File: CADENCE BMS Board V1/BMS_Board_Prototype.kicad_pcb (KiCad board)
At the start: 4 copper layers, 97 x 97 mm, 174 parts, among them IC1 R5432V407BA, J1 Screw_Terminal_01x02, J10 Conn_01x08, J11 Conn_01x06, J12 Conn_01x02, J13 Conn_01x08, J14 Conn_01x04, J15 Conn_01x08, J2 Conn_01x02, J20 Conn_01x02, J21 Conn_01x02, J28 Banana Socket PWR, J29 Banana Socket VSS, J3 Conn_01x08, J4 Conn_01x02, J5 Conn_01x01_Socket, J6 Conn_01x01_Socket, J7 Conn_01x01_Socket, J8 Conn_01x01_Socket, J9 Conn_01x04, Q1 P-Channel FET, Q10 N-MOS, Q2 60V Enhancement, Q3 60V Enhancement, Q4 60V Enhancement, Q5 Q_NMOS_DSG, Q6 Q_NMOS_DSG, Q7 Q_NMOS_DSG, Q8 N-MOS, Q9 N-MOS, U1 TVS2200DRV, U2 LT8612, U3 LT3652IMSE#PBF, U4 BQ34Z100-R2, U5 MCP9600-E_MX, U7 P82B715DR

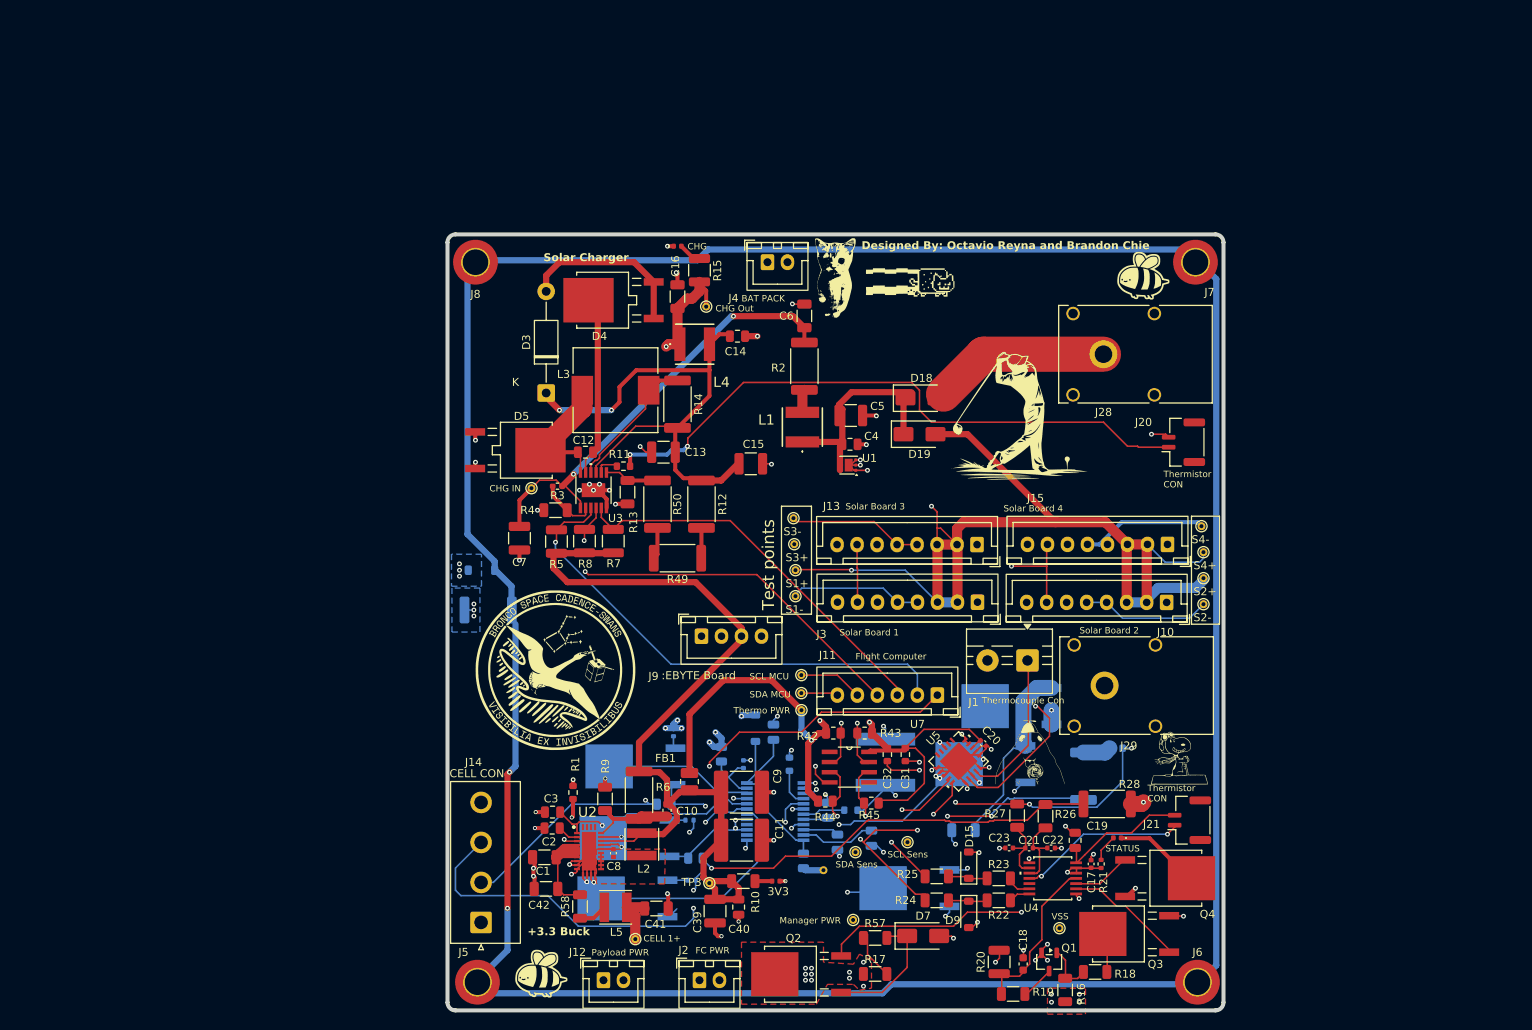
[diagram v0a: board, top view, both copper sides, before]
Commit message: Updates for USB-C charging and set up for testing
Revamped USB-C layout to make it cleaner and more compressed and also included schematic parts for adding in Banana plugs for testing the PCB
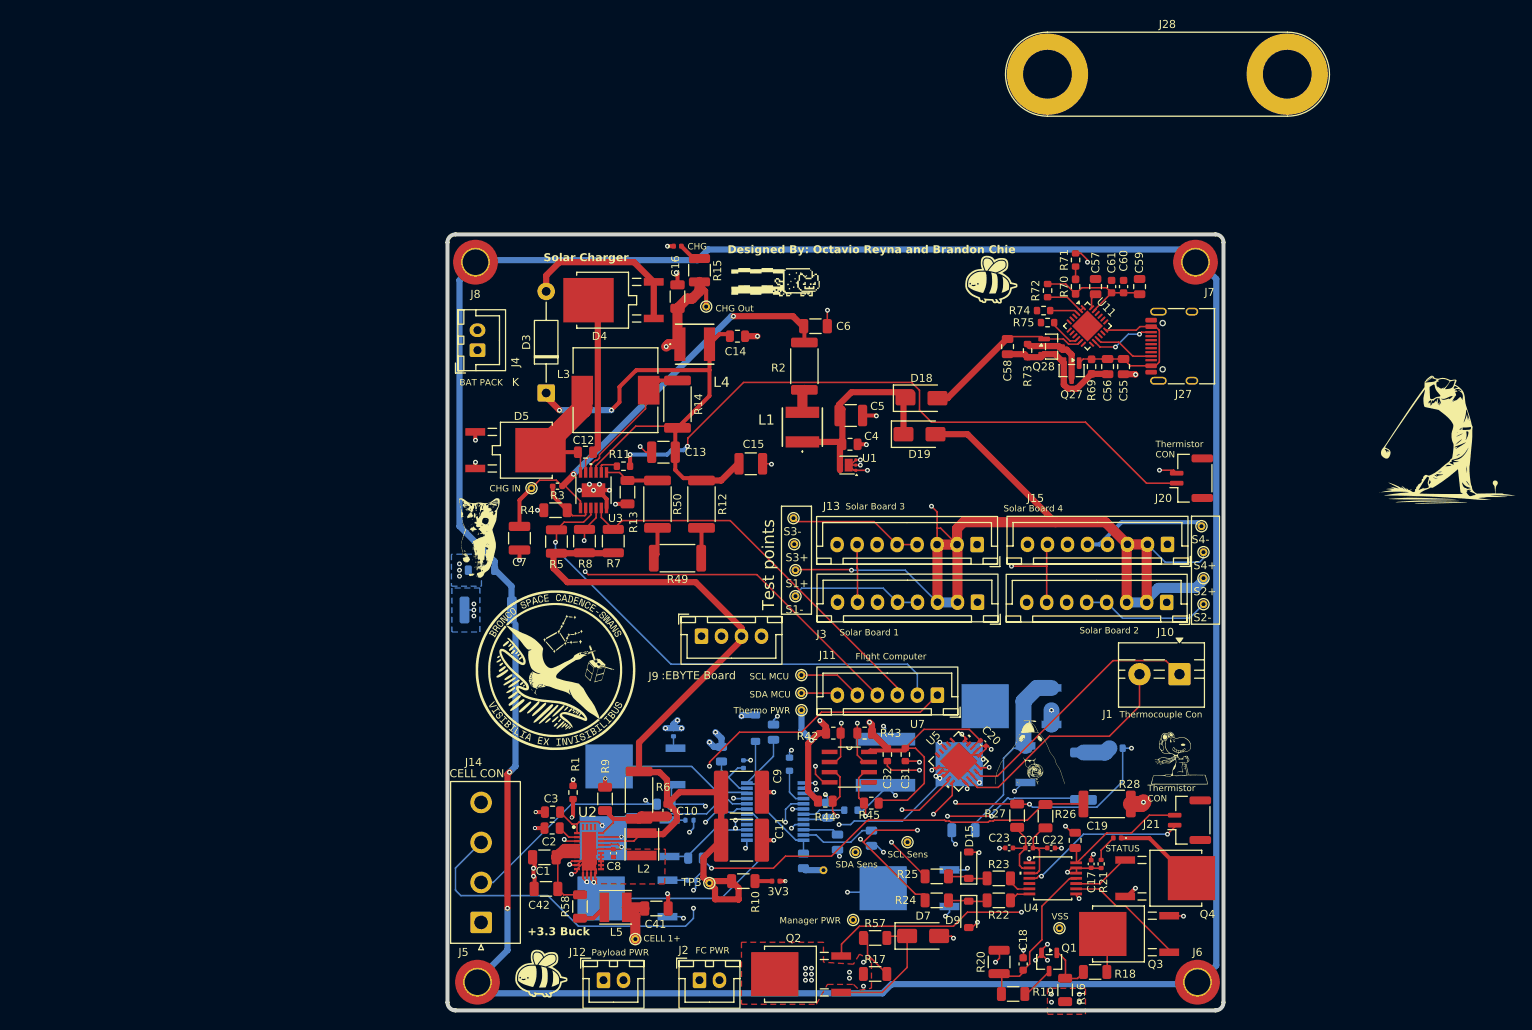
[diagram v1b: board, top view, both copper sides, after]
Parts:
- removed C39: 10uF, Capacitor_SMD:C_1210_3225Metric
- removed C40: 10nF, Capacitor_SMD:C_0805_2012Metric
- removed FB1: 600, Inductor_SMD:L_1008_2520Metric
- removed J29: Banana Socket VSS, Connector:Banana_Cliff_FCR7350B_S16N-PC_Horizontal
- added C55: 3.3uF, Capacitor_SMD:C_0805_2012Metric, F.Cu at (109.5, 36.5)
- added C56: 1uF, Capacitor_SMD:C_0805_2012Metric, F.Cu at (107.5, 36.5)
- added C57: 1uF, Capacitor_SMD:C_0805_2012Metric, F.Cu at (106.0, 26.5)
- added C58: 1uF, Capacitor_SMD:C_0805_2012Metric, F.Cu at (95.0, 34.0)
- added C59: 1uF, Capacitor_SMD:C_0805_2012Metric, F.Cu at (111.5, 26.5)
- added C60: 100nF, Capacitor_SMD:C_0603_1608Metric, F.Cu at (109.5, 26.5)
- added C61: 100nF, Capacitor_SMD:C_0603_1608Metric, F.Cu at (108.0, 26.5)
- added J27: USB_C_Receptacle_USB2.0_16P, Connector_USB:USB_C_Receptacle_HRO_TYPE-C-31-M-12, F.Cu at (117.0, 34.0)
- added Q27: Q_PMOS_DGS, Package_TO_SOT_SMD:SOT-23, F.Cu at (103.0, 37.0)
- added Q28: Q_PMOS_DGS, Package_TO_SOT_SMD:SOT-23, F.Cu at (100.5, 34.0)
- added R69: 10K, Resistor_SMD:R_0603_1608Metric_Pad0.98x0.95mm_HandSolder, F.Cu at (105.5, 36.5)
- added R70: 5.1K, Resistor_SMD:R_0603_1608Metric_Pad0.98x0.95mm_HandSolder, F.Cu at (103.5, 26.5)
- added R71: 2.4K, Resistor_SMD:R_0603_1608Metric, F.Cu at (103.5, 23.2)
- added R72: 0, Resistor_SMD:R_0603_1608Metric, F.Cu at (100.0, 27.0)
- added R73: 49.9K, Resistor_SMD:R_0603_1608Metric, F.Cu at (97.5, 34.5)
- added R74: 49.9K, Resistor_SMD:R_0603_1608Metric, F.Cu at (99.5, 29.5)
- added R75: 10K, Resistor_SMD:R_0603_1608Metric, F.Cu at (100.0, 31.0)
- added U11: CYPD3177-24LQ, Package_DFN_QFN:QFN-24-1EP_4x4mm_P0.5mm_EP2.75x2.75mm, F.Cu at (105.0, 31.5)
- J28: value Banana Socket PWR -> Banana Jack CON; footprint Connector:Banana_Cliff_FCR7350R_S16N-PC_Horizontal -> Connector:Banana_Jack_2Pin
- moved G*** 55.1 mm to (29.0, 58.0)
- moved G*** 53.6 mm to (149.5, 45.5)
- moved J4 37.9 mm to (28.8, 34.5), turned to 90 degrees
- moved J28 35.7 mm to (100.0, 0.00), turned to 0 degrees
- moved J1 19.1 mm to (116.5, 75.0)
- moved G*** 19.0 mm to (93.0, 25.5)
- moved G*** 16.8 mm to (65.2, 25.7)
- moved J20 4.61 mm to (118.0, 50.5)
- moved C6 1.89 mm to (71.0, 31.5), turned to 0 degrees
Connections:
- C20 pad 2: +3.3V Q -> +3.3V
- C31 pad 1: +3.3V Q -> +3.3V
- C32 pad 1: +3.3V Q -> +3.3V
- D18 pad 2: Net-(D18-A) -> VDC_OUT
- J28 pad 1: Net-(D18-A) -> Cell 3-
- R42 pad 1: +3.3V Q -> +3.3V
- R43 pad 1: +3.3V Q -> +3.3V
- R44 pad 1: +3.3V Q -> +3.3V
- R45 pad 1: +3.3V Q -> +3.3V
- TP7 pad 1: +3.3V Q -> +3.3V
- U5 pad 8: +3.3V Q -> +3.3V
- U7 pad 8: +3.3V Q -> +3.3V
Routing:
- net +3.3V Q: track 81.9 -> 0.00 mm, vias 3 -> 0
- net +3.3V: track 112.8 -> 163.4 mm, vias 0 -> 3
- net Net-(D18-A): track 22.1 -> 0.00 mm
- net VDC_OUT: track 0.00 -> 21.6 mm
- net VBUS: track 0.00 -> 21.3 mm
- net Net-(Q27-G): track 0.00 -> 16.9 mm
- net VDDD: track 0.00 -> 15.8 mm
- net Net-(J1-Pin_1): track 19.0 -> 32.4 mm
- net Net-(Q27-S): track 0.00 -> 8.99 mm
- net CC2: track 0.00 -> 8.14 mm, vias 0 -> 2
- net CC1: track 0.00 -> 7.65 mm
- net Net-(U11-VBUS_MAX): track 0.00 -> 5.31 mm
- net Net-(U11-FLIP): track 0.00 -> 4.20 mm
- net Net-(J1-Pin_2): track 26.3 -> 30.0 mm, vias 1 -> 0
- net VBUS_EN: track 0.00 -> 3.59 mm
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
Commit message: New connectors and adding in a test setup
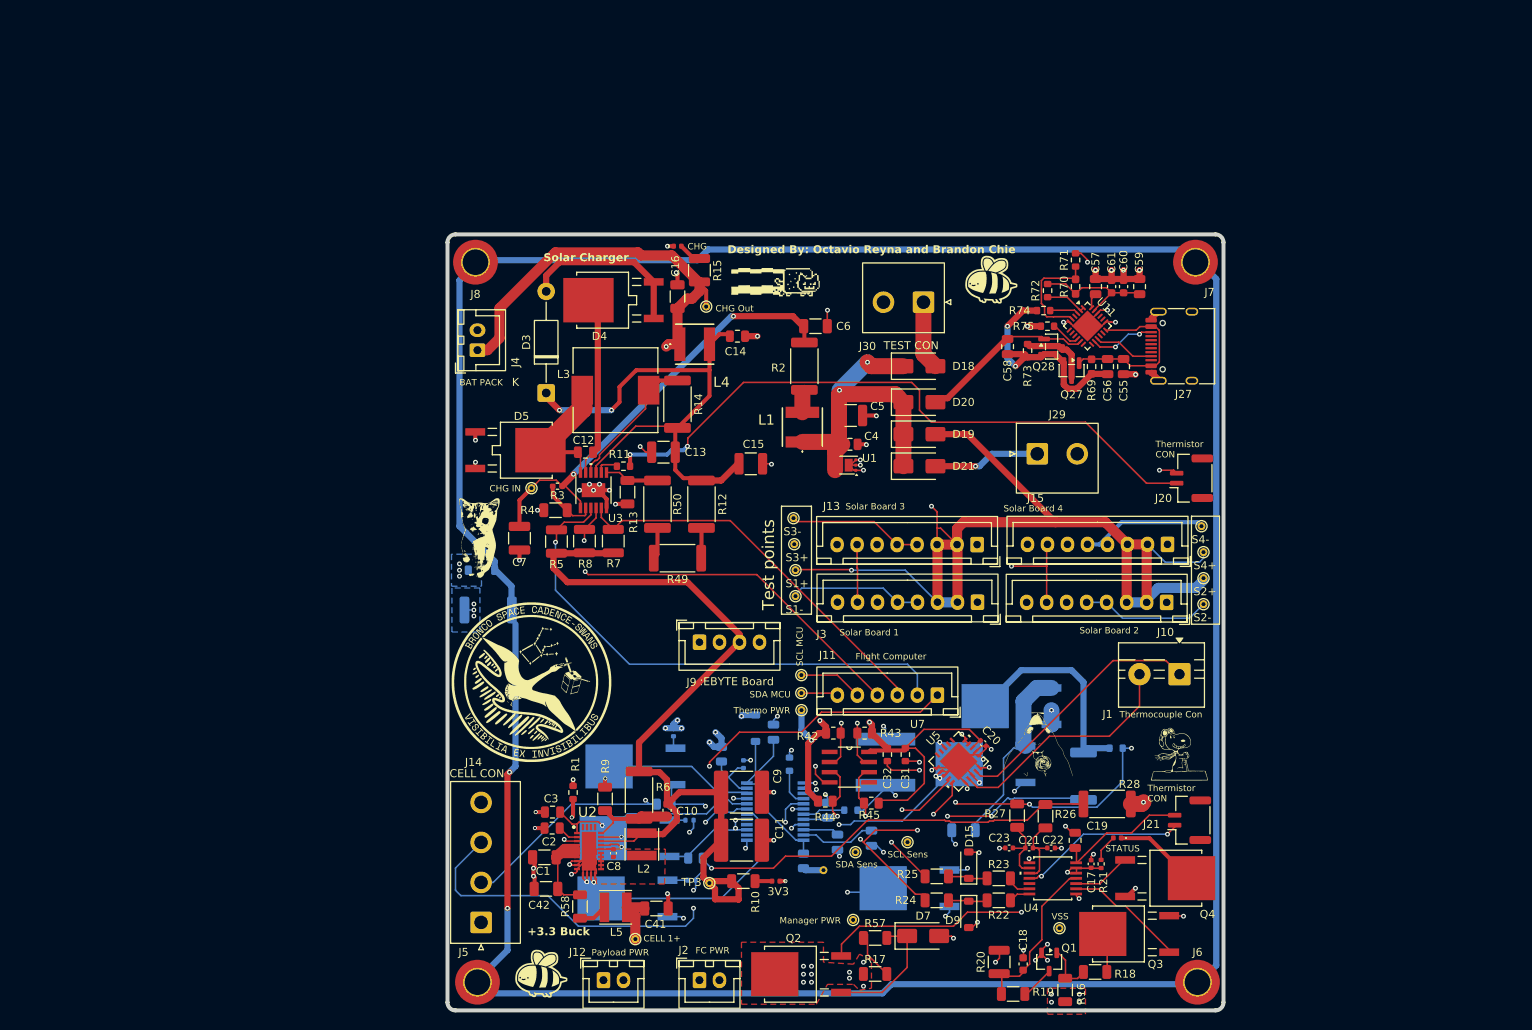
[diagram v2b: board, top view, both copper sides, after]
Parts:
- removed the G*** at (149.5, 45.5)
- removed J28: Banana Jack CON, Connector:Banana_Jack_2Pin
- added D20: D_Schottky 40v, Diode_SMD:D_SMA, F.Cu at (84.0, 41.0)
- added D21: D_Schottky 40v, Diode_SMD:D_SMA, F.Cu at (84.0, 49.0)
- added J29: Conn_01x02, Connector_JST:JST_NV_B02P-NV_1x02_P5.00mm_Vertical, F.Cu at (98.7, 47.5)
- added J30: Conn_01x02, Connector_JST:JST_NV_B02P-NV_1x02_P5.00mm_Vertical, F.Cu at (84.5, 28.5)
- moved D18 4.01 mm to (84.0, 36.5)
- moved G*** 3.35 mm to (35.5, 76.0)
- moved G*** 1.41 mm to (98.5, 83.5)
- moved J9 0.79 mm to (56.5, 71.0)
- moved G*** 0.50 mm to (116.5, 83.9)
- moved R75 0.45 mm to (100.0, 31.5)
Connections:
- C1 pad 2: Cell 3- -> VSS
- C11 pad 1: Cell 3- -> VSS
- C13 pad 2: Cell 3- -> VSS
- C14 pad 2: Cell 3- -> VSS
- C15 pad 2: Cell 3- -> VSS
- C16 pad 2: Cell 3- -> VSS
- C17 pad 2: Cell 3- -> VSS
- C18 pad 1: Cell 3- -> VSS
- C19 pad 1: Cell 3- -> VSS
- C2 pad 1: Cell 3- -> VSS
- C20 pad 1: Cell 3- -> VSS
- C22 pad 1: Cell 3- -> VSS
- C23 pad 1: Cell 3- -> VSS
- C24 pad 1: Cell 3- -> VSS
- C25 pad 2: Cell 3- -> VSS
- C26 pad 1: Cell 3- -> VSS
- C3 pad 1: Cell 3- -> VSS
- C31 pad 2: Cell 3- -> VSS
- C32 pad 2: Cell 3- -> VSS
- C4 pad 2: Cell 3- -> VSS
- C41 pad 1: Cell 1+ -> UNREG
- C41 pad 2: Cell 3- -> VSS
- C42 pad 2: Cell 3- -> VSS
- C43 pad 2: Cell 3- -> VSS
- C5 pad 2: Cell 3- -> VSS
- C55 pad 2: Cell 3- -> VSS
- C57 pad 1: Cell 3- -> VSS
- C59 pad 2: Cell 3- -> VSS
- C6 pad 1: Net-(U3-VIN) -> V_mppt_i
- C6 pad 2: Cell 3- -> VSS
- C60 pad 2: Cell 3- -> VSS
- C61 pad 2: Cell 3- -> VSS
- C7 pad 1: Net-(U3-VIN) -> V_mppt_o
- C7 pad 2: Cell 3- -> VSS
- C9 pad 1: Cell 3- -> VSS
- D15 pad 2: Cell 3- -> VSS
- D18 pad 2: VDC_OUT -> TEST_PWR
- D2 pad 1: Cell 3- -> VSS
- D5 pad 1: Cell 3- -> VSS
- D6 pad 1: Cell 3- -> VSS
- D7 pad 2: Cell 3- -> VSS
- D9 pad 2: Cell 3- -> VSS
- IC1 pad 9: Cell 3- -> VSS
- J10 pad 4: Cell 3- -> VSS
- J10 pad 5: Cell 3- -> Solar1-
- J10 pad 6: Cell 3- -> Solar1-
- J12 pad 1: Cell 1+ -> UNREG
- J12 pad 2: Cell 3- -> VSS
- J13 pad 4: Cell 3- -> VSS
- J13 pad 5: Cell 3- -> Solar1-
- J13 pad 6: Cell 3- -> Solar1-
- J15 pad 4: Cell 3- -> VSS
- J15 pad 5: Cell 3- -> Solar1-
- J15 pad 6: Cell 3- -> Solar1-
- J2 pad 1: Cell 1+ -> UNREG
- J2 pad 2: Cell 3- -> VSS
- J20 pad 2: Cell 3- -> VSS
- J27 pad A1: Cell 3- -> VSS
- J27 pad A12: Cell 3- -> VSS
- J27 pad B1: Cell 3- -> VSS
- J27 pad B12: Cell 3- -> VSS
- J27 pad SH: Cell 3- -> VSS
- J3 pad 4: Cell 3- -> VSS
- J3 pad 5: Cell 3- -> Solar1-
- J3 pad 6: Cell 3- -> Solar1-
- J4 pad 2: Cell 3- -> VSS
- J9 pad 1: Cell 1+ -> UNREG
- J9 pad 2: Cell 3- -> VSS
- J9 pad 4: Cell 3- -> VSS
- L5 pad 1: Cell 1+ -> UNREG
- Q1 pad 2: Cell 1+ -> UNREG
- Q2 pad 3: Cell 1+ -> UNREG
- Q3 pad 2: Cell 3- -> VSS
- Q4 pad 2: Cell 3- -> VSS
- Q5 pad 2: Cell 3- -> VSS
- R1 pad 2: Cell 3- -> VSS
- R13 pad 2: Cell 3- -> VSS
- R16 pad 1: Cell 1+ -> UNREG
- R17 pad 1: Cell 1+ -> UNREG
- R2 pad 2: Net-(U3-VIN) -> V_mppt_i
- R20 pad 2: Cell 3- -> VSS
- R3 pad 1: Net-(U3-VIN) -> V_mppt_o
- R31 pad 1: Cell 3- -> VSS
- R35 pad 1: Cell 1+ -> UNREG
- R4 pad 2: Cell 3- -> VSS
- R59 pad 2: Cell 3- -> VSS
- R71 pad 2: Cell 3- -> VSS
- R9 pad 2: Cell 3- -> VSS
- TP1 pad 1: Cell 1+ -> UNREG
- TP12 pad 1: Cell 3- -> Solar1-
- TP14 pad 1: Cell 3- -> Solar1-
- TP16 pad 1: Cell 3- -> Solar1-
- TP2 pad 1: Net-(U3-VIN) -> V_mppt_o
- TP5 pad 1: Cell 1+ -> UNREG
- TP6 pad 1: Cell 3- -> VSS
- TP8 pad 1: Cell 1+ -> UNREG
- TP9 pad 1: Cell 3- -> Solar1-
- U1 pad 1: Cell 3- -> VSS
- U1 pad 2: Cell 3- -> VSS
- U1 pad 3: Cell 3- -> VSS
- U1 pad 7: Cell 3- -> VSS
- U11 pad 19: Cell 3- -> VSS
- U11 pad 22: Cell 3- -> VSS
- U11 pad 25: Cell 3- -> VSS
- U11 pad 6: Cell 3- -> VSS
- U2 pad 10: Cell 3- -> VSS
- U2 pad 11: Cell 3- -> VSS
- U2 pad 12: Cell 3- -> VSS
- U2 pad 13: Cell 3- -> VSS
- U2 pad 14: Cell 3- -> VSS
- U2 pad 29: Cell 3- -> VSS
- U2 pad 8: Cell 3- -> VSS
- U2 pad 9: Cell 3- -> VSS
- U3 pad 1: Net-(U3-VIN) -> V_mppt_o
- U3 pad 13: Cell 3- -> VSS
- U3 pad 6: Cell 3- -> VSS
- U4 pad 1: Cell 3- -> VSS
- U4 pad 8: Cell 3- -> VSS
- U5 pad 1: Cell 3- -> VSS
- U5 pad 10: Cell 3- -> VSS
- U5 pad 13: Cell 3- -> VSS
- U5 pad 16: Cell 3- -> VSS
- U5 pad 17: Cell 3- -> VSS
- U5 pad 18: Cell 3- -> VSS
- U5 pad 21: Cell 3- -> VSS
- U5 pad 3: Cell 3- -> VSS
- U5 pad 5: Cell 3- -> VSS
- U5 pad 6: Cell 3- -> VSS
- U5 pad 7: Cell 3- -> VSS
- U5 pad 9: Cell 3- -> VSS
- U7 pad 4: Cell 3- -> VSS
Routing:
- net Cell 3-: track 292.6 -> 78.0 mm, vias 89 -> 13
- net VSS: track 0.00 -> 171.4 mm, vias 0 -> 78
- net Solar1-: track 0.00 -> 66.1 mm, vias 0 -> 5
- net Net-(U3-VIN): track 55.3 -> 0.00 mm, vias 2 -> 0
- net (no net): track 0.00 -> 55.3 mm, vias 0 -> 2
- net Cell 1+: track 34.9 -> 58.3 mm, vias 23 -> 16
- net Net-(Q6-G): track 3.47 -> 26.7 mm
- net USB PWR: track 0.00 -> 13.4 mm, vias 0 -> 1
- net UNREG: track 0.00 -> 13.2 mm, vias 0 -> 7
- net Net-(U11-ISNK_COARSE): track 1.59 -> 14.1 mm
- net Net-(Q27-G): track 16.9 -> 28.8 mm, vias 0 -> 2
- net Net-(D18-K): track 28.4 -> 40.1 mm, vias 0 -> 2
- net TEST_PWR: track 0.00 -> 8.62 mm
- net SHDN': track 62.7 -> 65.7 mm
- net +3.3V: track 163.4 -> 164.2 mm, vias 3 -> 4
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- added copper zone on B.Cu, net Solar1-
- added copper zone on F.Cu, net UNREG
- added copper zone on In2.Cu, net UNREG
- added copper zone on In1.Cu, net VSS
- removed copper zone on In2.Cu, net Cell 1+
- removed copper zone on B.Cu, net Cell 3-
- removed copper zone on In1.Cu, net Cell 3-
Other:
- board text added: "TEST CON"

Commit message: Updates to incorporate inhibit board
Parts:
- removed C14: 10nF, Capacitor_SMD:C_0805_2012Metric
- removed C15: 10uF, Capacitor_SMD:C_1210_3225Metric
- removed C16: 4.7uF, Capacitor_SMD:C_1206_3216Metric
- removed L4: 4.7u, FNR5040S4R7MT:FNR5040S4R7MT
- added J28: Conn_01x02, Connector_JST:JST_XH_B2B-XH-A_1x02_P2.50mm_Vertical, F.Cu at (-15.8, 64.5)
- added J31: Conn_01x04, Connector_JST:JST_XH_B4B-XH-A_1x04_P2.50mm_Vertical, F.Cu at (-26.0, 45.9)
- R12, R49, R50: footprint Resistor_SMD:R_2512_6332Metric -> Resistor_SMD:R_0603_1608Metric
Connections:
- C13 pad 1: Net-(D3-K) -> Cell 1+
- D3 pad 1: Net-(D3-K) -> Cell 1+
- R12 pad 1: Net-(D3-K) -> Cell 1+
- R14 pad 2: Net-(D3-K) -> Cell 1+
- U3 pad 9: Net-(D3-K) -> Cell 1+
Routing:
- net Cell 1+: track 58.3 -> 181.3 mm, vias 16 -> 15
- net Net-(D3-K): track 72.5 -> 0.00 mm, vias 2 -> 0
- net Cell 3-: track 78.0 -> 118.6 mm
- net Solar1-: track 66.1 -> 72.3 mm, vias 5 -> 0
- net VSS: track 171.4 -> 169.9 mm, vias 78 -> 82
- net V_mppt_o: track 0.00 -> 1.55 mm, vias 0 -> 1
- net UNREG: vias 7 -> 11
- added copper zone on B.Cu, net VSS
- removed copper zone on B.Cu, net Solar1-
